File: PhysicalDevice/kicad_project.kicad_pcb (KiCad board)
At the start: 2 copper layers, 100 x 50 mm, 22 parts, among them J1 Conn_01x06, J2 USB_B_Micro, SW1 SW_Push, SW2 SW_Push, SW3 SW_Push, U1 MAX7219CWGT, U3 AMS1117-3.3

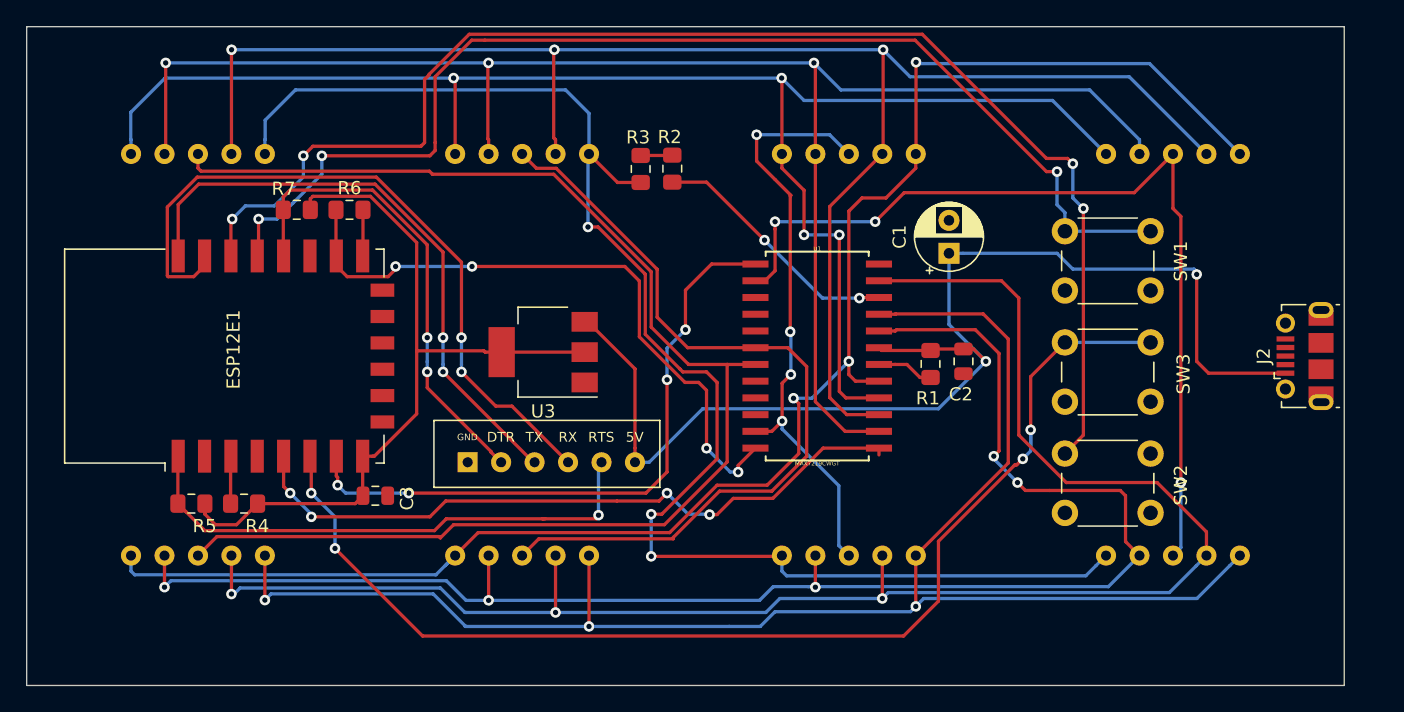
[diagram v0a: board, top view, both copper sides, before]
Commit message: Board fully routed. Gerber file generated.
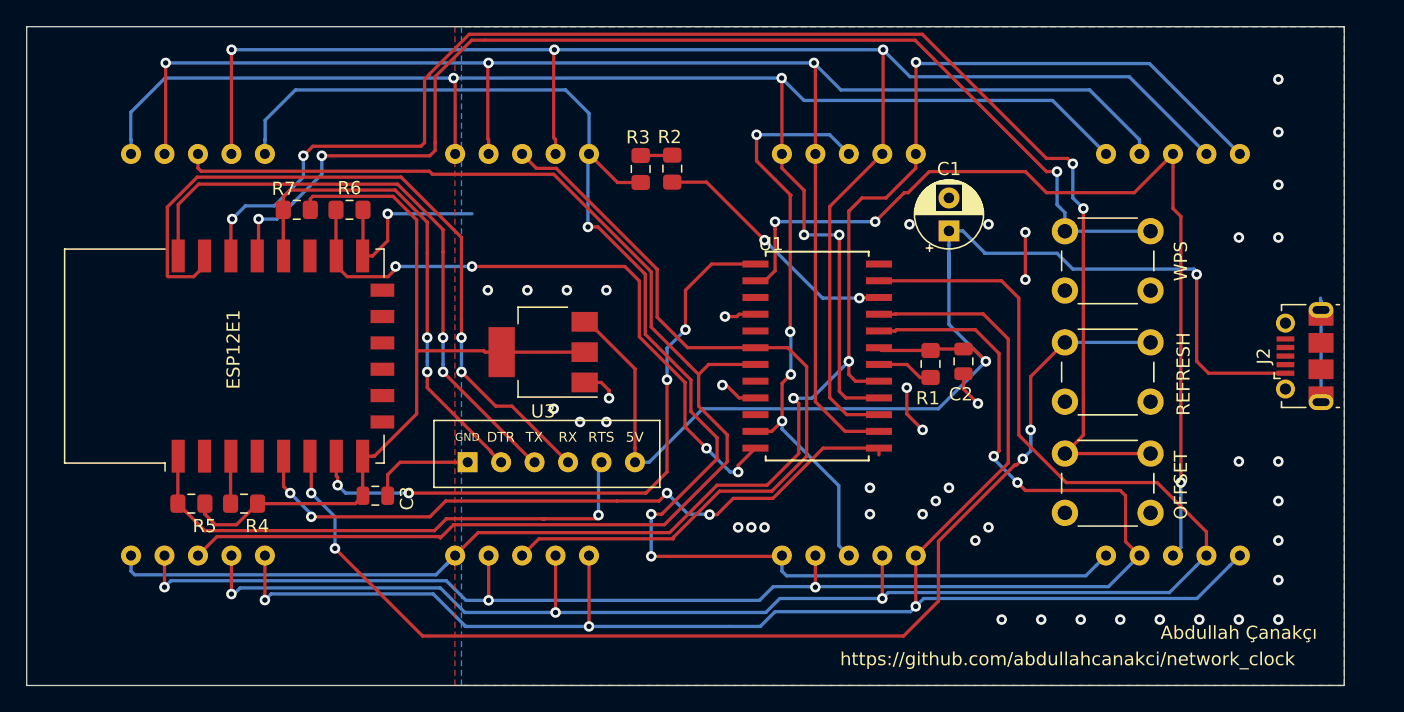
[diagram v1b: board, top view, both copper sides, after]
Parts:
- moved C1 1.70 mm to (70.0, 15.5)
- renumbered SW2 to OFFSET, SW3 to REFRESH, SW1 to WPS
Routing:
- net GNDREF: track 3.51 -> 44.7 mm, vias 0 -> 44
- net /BUT_REFRESH: track 103.2 -> 109.7 mm
- net +5V: track 93.5 -> 97.7 mm
- net (no net): track 0.00 -> 3.60 mm, vias 0 -> 2
- net /DIG_0: track 68.8 -> 70.2 mm
- net Net-(ESP12E1-Pad21): track 54.4 -> 55.5 mm
- net /SEG_DP: track 111.9 -> 110.9 mm
- net +3V3: track 58.7 -> 59.7 mm
- net Net-(ESP12E1-Pad22): track 45.7 -> 46.7 mm
- net Net-(ESP12E1-Pad18): track 36.2 -> 37.2 mm
- net /DIG_3: track 102.6 -> 103.4 mm
- net /LOAD_3V3: track 49.4 -> 48.8 mm
- added copper zone on B.Cu, net GNDREF
- added copper zone on F.Cu, net GNDREF
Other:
- board text added: "Abdullah Çanakçı"
- board text added: "https://github.com/abdullahcanakci/network_clock"

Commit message: added leds and rerouted some bits to be more tidy
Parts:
- added LED1: CONN, LED_SMD:LED_0805_2012Metric_Pad1.15x1.40mm_HandSolder, B.Cu at (85.8, 3.10)
- added LED2: WPS, LED_SMD:LED_0805_2012Metric_Pad1.15x1.40mm_HandSolder, B.Cu at (90.2, 3.10)
- added R8: 220R, Resistor_SMD:R_0805_2012Metric_Pad1.15x1.40mm_HandSolder, F.Cu at (48.3, 14.7)
- added R9: 2204, Resistor_SMD:R_0805_2012Metric_Pad1.15x1.40mm_HandSolder, F.Cu at (44.2, 14.7)
- renumbered WPS to SW1, OFFSET to SW2, REFRESH to SW3
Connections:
- ESP12E1 pad 17: Net-(ESP12E1-Pad17) -> /LED_CONN
- ESP12E1 pad 4: Net-(ESP12E1-Pad4) -> /LED_WPS
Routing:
- net /LED_WPS: track 0.00 -> 58.7 mm, vias 0 -> 6
- net Net-(R8-Pad1): track 0.00 -> 54.9 mm, vias 0 -> 6
- net Net-(CONN1-Pad2): track 0.00 -> 51.6 mm, vias 0 -> 4
- net /LED_CONN: track 0.00 -> 30.0 mm, vias 0 -> 5
- net /SEG_A: track 122.8 -> 110.7 mm
- net /SEG_DP: track 110.9 -> 120.5 mm, vias 3 -> 4
- net /SEG_F: track 125.5 -> 116.0 mm
- net /SEG_B: track 116.8 -> 107.9 mm
- net /DIG_2: track 62.0 -> 69.5 mm
- net /CLOCK_3V3: track 52.6 -> 59.9 mm, vias 4 -> 2
- net /SEG_G: track 124.1 -> 116.8 mm
- net /BUT_WPS: track 88.6 -> 84.4 mm
- net /BUT_REFRESH: track 109.7 -> 105.8 mm
- net /SEG_E: track 120.0 -> 117.3 mm
- net /SEG_D: track 127.9 -> 125.3 mm
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
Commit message: pre track witdh change
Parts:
- added SW4: SW_Push, KicadLibrary:DTS-3, F.Cu at (82.2, 31.8)
- CONN1: renamed from LED1; value CONN -> LED
- SW1, SW2, SW3: footprint Button_Switch_THT:SW_PUSH_6mm -> KicadLibrary:DTS-3
- WPS1: renamed from LED2; value WPS -> LED
- moved SW2 7.20 mm to (82.2, 26.1)
- moved SW3 4.95 mm to (82.2, 20.4)
- moved SW1 3.54 mm to (82.2, 14.8)
- moved R2 2.76 mm to (51.5, 11.8), turned to 180 degrees
- moved R3 1.21 mm to (47.2, 11.8), turned to 0 degrees
- moved U3 1.17 mm to (40.0, 23.8), turned to 90 degrees
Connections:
- net Net-(ESP12E1-Pad1) renamed /BUT_RST
- DIG0 pad 3: /DIG_0 -> Net-(DIG0-Pad3)
- DIG0 pad 8: /DIG_0 -> GNDREF
- DIG1 pad 8: /DIG_1 -> Net-(DIG1-Pad8)
- DIG2 pad 3: /DIG_2 -> Net-(DIG2-Pad3)
- DIG3 pad 3: /DIG_3 -> Net-(DIG3-Pad3)
- U1 pad 10: /DIG_5 -> GNDREF
- U1 pad 2: /DIG_0 -> GNDREF
- U1 pad 3: /DIG_4 -> GNDREF
- U1 pad 8: /DIG_7 -> GNDREF
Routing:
- net /DIG_0: track 70.2 -> 0.00 mm, vias 3 -> 0
- net /DIG_3: track 103.6 -> 57.9 mm
- net /BUT_RST: track 41.2 -> 83.1 mm, vias 1 -> 3
- net /DIG_2: track 69.5 -> 33.6 mm
- net /DIG_1: track 45.1 -> 12.8 mm, vias 4 -> 2
- net GNDREF: track 44.7 -> 72.5 mm, vias 33 -> 19
- net /SEG_DP: track 120.5 -> 93.8 mm, vias 4 -> 3
- net /SEG_G: track 116.8 -> 128.1 mm, vias 3 -> 4
- net /BUT_REFRESH: track 105.8 -> 95.1 mm
- net /BUT_WPS: track 84.4 -> 78.5 mm, vias 3 -> 2
- net /BUT_OFFSET: track 89.3 -> 84.0 mm, vias 4 -> 2
- net /MOSI_3V3: track 49.4 -> 54.5 mm, vias 4 -> 2
- net (no net): track 3.60 -> 0.00 mm, vias 2 -> 0
- net +3V3: track 59.7 -> 56.5 mm
- net /LED_CONN: track 30.0 -> 33.2 mm, vias 5 -> 2
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- added copper zone on F.Cu, net +3V3
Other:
- net class Default: clearance 0.2 -> 0.3; trace_width 0.25 -> 0.35
- rule trace_clearance: 0.2 -> 0.3
- board text added: "MAX7219CWG"

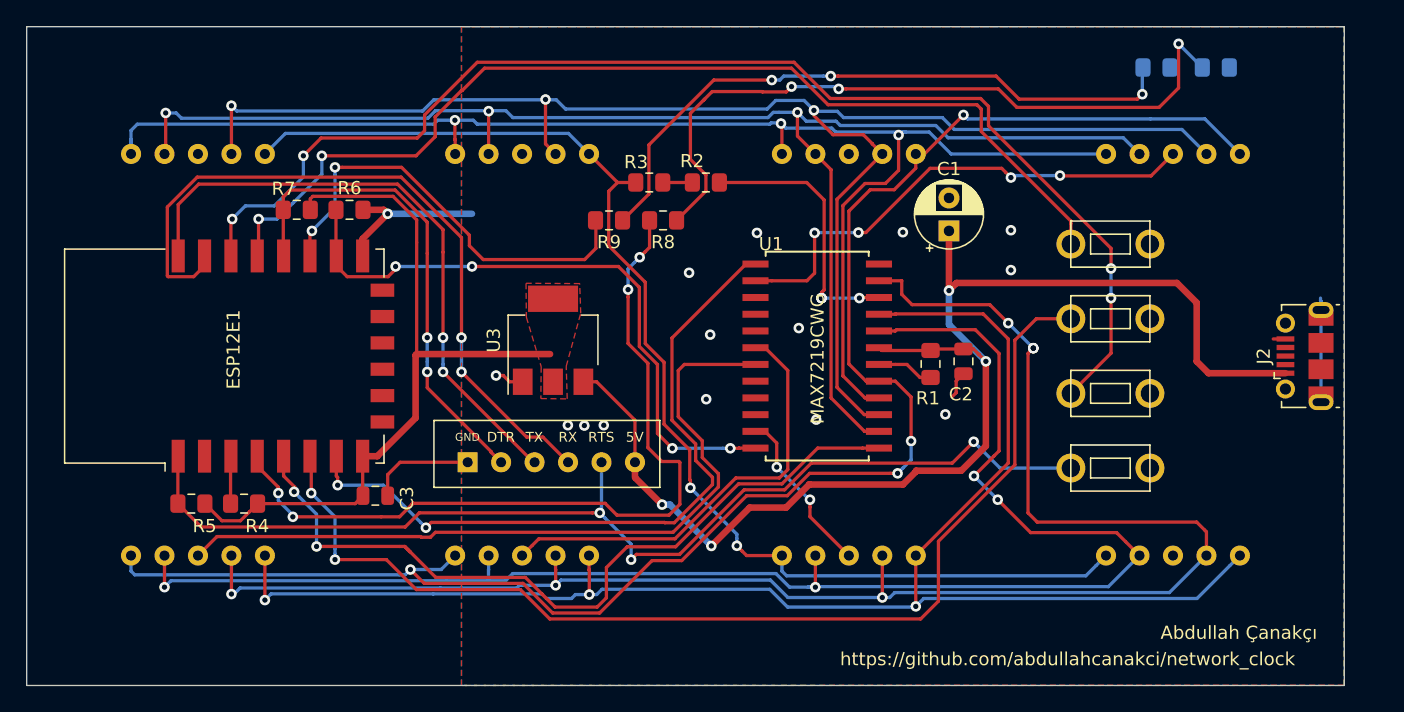
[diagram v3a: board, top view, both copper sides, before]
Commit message: changed min routing size from 0.25mm(~9.8mil) to 0.35(~13.4mil)
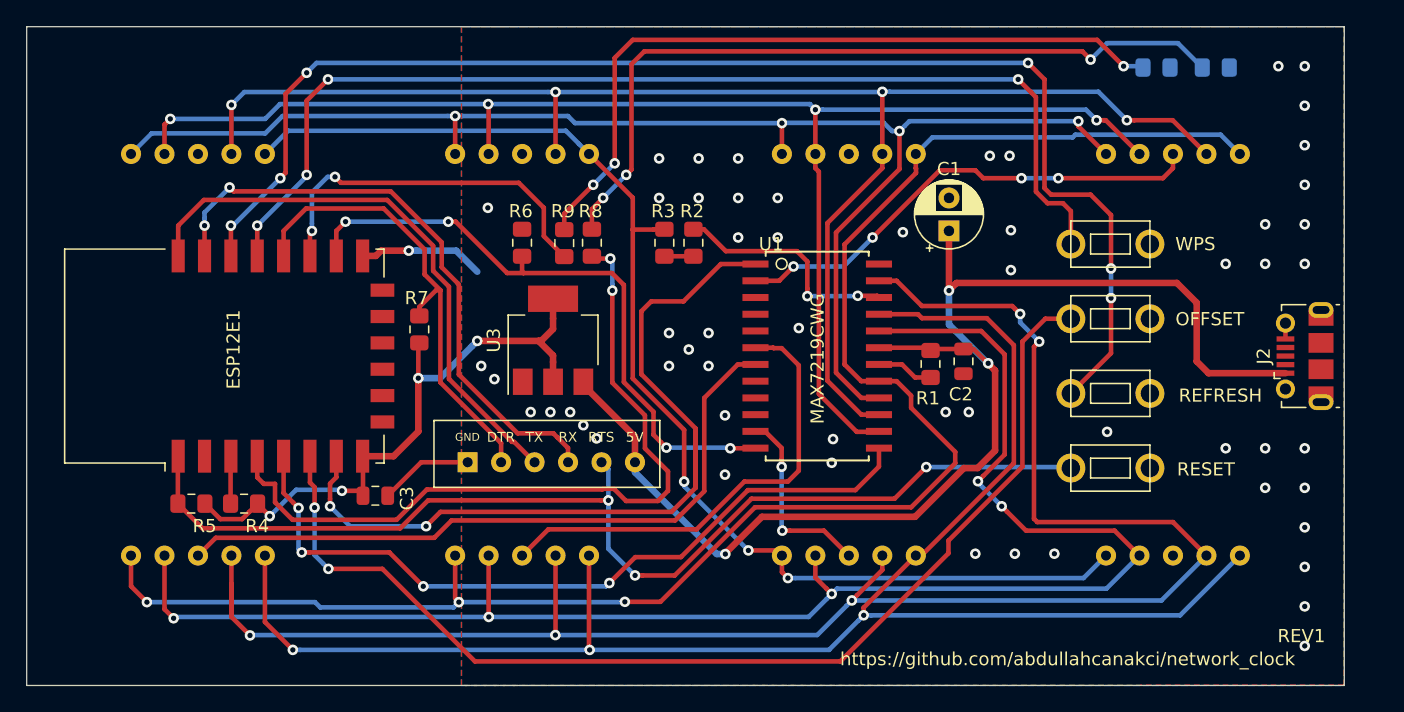
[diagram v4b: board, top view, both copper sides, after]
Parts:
- LED1: renamed from WPS1; value LED -> WPS
- LED2: renamed from CONN1; value LED -> CONN
- moved R6 13.3 mm to (37.6, 16.4), turned to 90 degrees
- moved R7 13.0 mm to (29.8, 23.0), turned to 90 degrees
- moved R8 5.66 mm to (42.9, 16.4), turned to 270 degrees
- moved R3 4.72 mm to (48.4, 16.4), turned to 270 degrees
- moved R2 4.67 mm to (50.6, 16.4), turned to 270 degrees
- moved R9 3.81 mm to (40.8, 16.4), turned to 270 degrees
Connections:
- DIG0 pad 8: GNDREF -> /DIG_0
- U1 pad 2: GNDREF -> /DIG_0
- U1 pad 5: /DIG_6 -> GNDREF
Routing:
- net GNDREF: track 72.5 -> 17.8 mm, vias 19 -> 58
- net /DIG_0: track 0.00 -> 36.8 mm, vias 0 -> 4
- net /SEG_E: track 117.0 -> 126.7 mm
- net +3V3: track 56.5 -> 47.0 mm, vias 0 -> 4
- net Net-(ESP12E1-Pad21): track 55.5 -> 46.1 mm
- net /SEG_D: track 127.7 -> 137.0 mm, vias 6 -> 5
- net /MOSI_3V3: track 54.5 -> 63.3 mm
- net Net-(LED2-Pad2): track 49.1 -> 56.1 mm
- net /BUT_REFRESH: track 95.1 -> 102.1 mm, vias 4 -> 6
- net /SEG_C: track 118.1 -> 123.8 mm, vias 4 -> 5
- net /DIG_3: track 57.9 -> 52.5 mm
- net /LED_CONN: track 33.2 -> 28.3 mm
- net /BUT_WPS: track 78.5 -> 82.8 mm, vias 2 -> 4
- net Net-(LED1-Pad2): track 54.7 -> 59.0 mm
- net /LED_WPS: track 61.0 -> 57.5 mm, vias 4 -> 2
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- removed copper zone on F.Cu, net +3V3
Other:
- net class 5V added: clearance 0.3, trace_width 0.5, via_dia 0.8, via_drill 0.4
- net class tight added: clearance 0.2, trace_width 0.35, via_dia 0.8, via_drill 0.4
- rule trace_min: 0.2 -> 0.34
- board text added: "REV1"
- board text removed: "Abdullah Çanakçı"
